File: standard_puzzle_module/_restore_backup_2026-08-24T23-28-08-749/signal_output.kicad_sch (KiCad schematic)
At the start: 6 parts

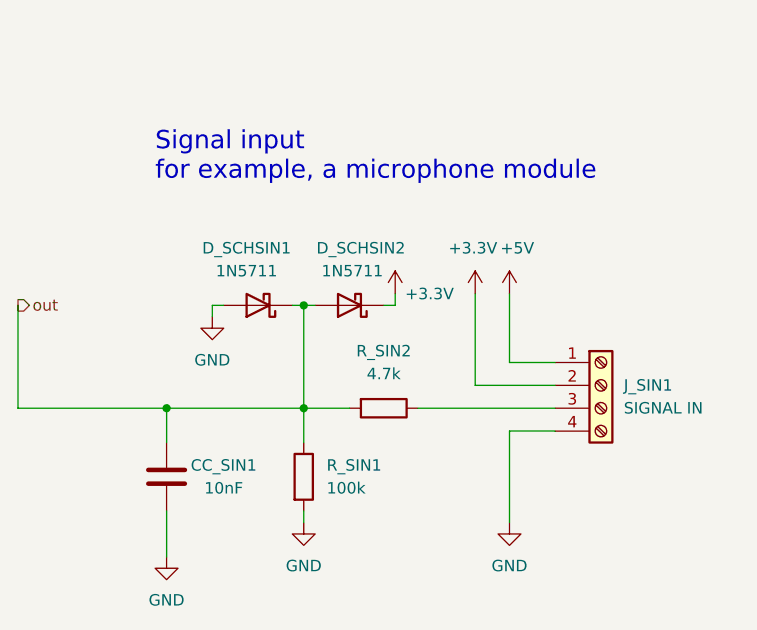
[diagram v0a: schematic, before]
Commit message: feat: draft component placement for pcb
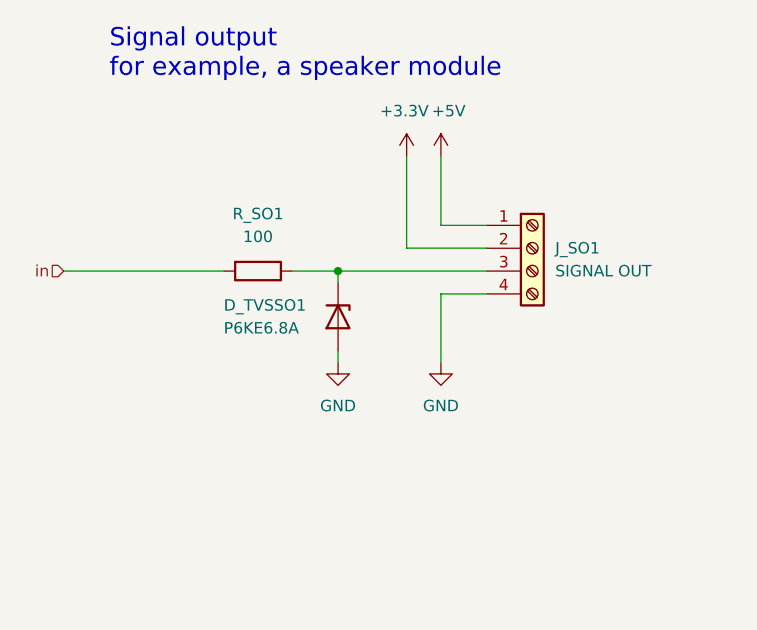
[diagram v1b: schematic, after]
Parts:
- removed CC_SIN1: 10nF, Capacitor_THT:C_Disc_D5.0mm_W2.5mm_P5.00mm, symbol Device:C
- removed D_SCHSIN1, D_SCHSIN2: 1N5711, Diode_THT:D_DO-35_SOD27_P7.62mm_Horizontal, symbol Diode:1N5711
- removed J_SIN1: SIGNAL IN, TerminalBlock_Phoenix:TerminalBlock_Phoenix_MKDS-1,5-4-5.08_1x04_P5.08mm_Horizontal, symbol Connector:Screw_Terminal_01x04
- removed R_SIN1: 100k, Resistor_THT:R_Axial_DIN0411_L9.9mm_D3.6mm_P15.24mm_Horizontal, symbol Device:R
- removed R_SIN2: 4.7k, Resistor_THT:R_Axial_DIN0411_L9.9mm_D3.6mm_P15.24mm_Horizontal, symbol Device:R
- added D_TVSSO1: P6KE6.8A, Diode_THT:D_DO-15_P12.70mm_Horizontal, symbol Diode:PTVS5V0Z1USK
- added J_SO1: SIGNAL OUT, TerminalBlock_Phoenix:TerminalBlock_Phoenix_MKDS-1,5-4-5.08_1x04_P5.08mm_Horizontal, symbol Connector:Screw_Terminal_01x04
- added R_SO1: 100, Resistor_THT:R_Axial_DIN0207_L6.3mm_D2.5mm_P10.16mm_Horizontal, symbol Device:R
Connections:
- net +3.3V: now also J_SO1.2 (Pin_2)
- net +5V: now also J_SO1.1 (Pin_1)
- net GND: now also D_TVSSO1.2 (A), J_SO1.4 (Pin_4)
- new net: D_TVSSO1.1 (K), J_SO1.3 (Pin_3), R_SO1.1
- new net in: R_SO1.2
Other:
- note added: "Signal output for example, a speaker module"
- note removed: "Signal input for example, a microphone module"
- title: Signal input -> ESP digital signal output (like a speaker module)
